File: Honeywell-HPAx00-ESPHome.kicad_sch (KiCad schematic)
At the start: 29 parts, among them J1 Conn_01x06, J2 Conn_01x01, J3 Conn_01x01, J4 Conn_01x01, J5 Conn_01x01, J6 Conn_01x01, J7 Conn_01x01, U1 mini_esp32

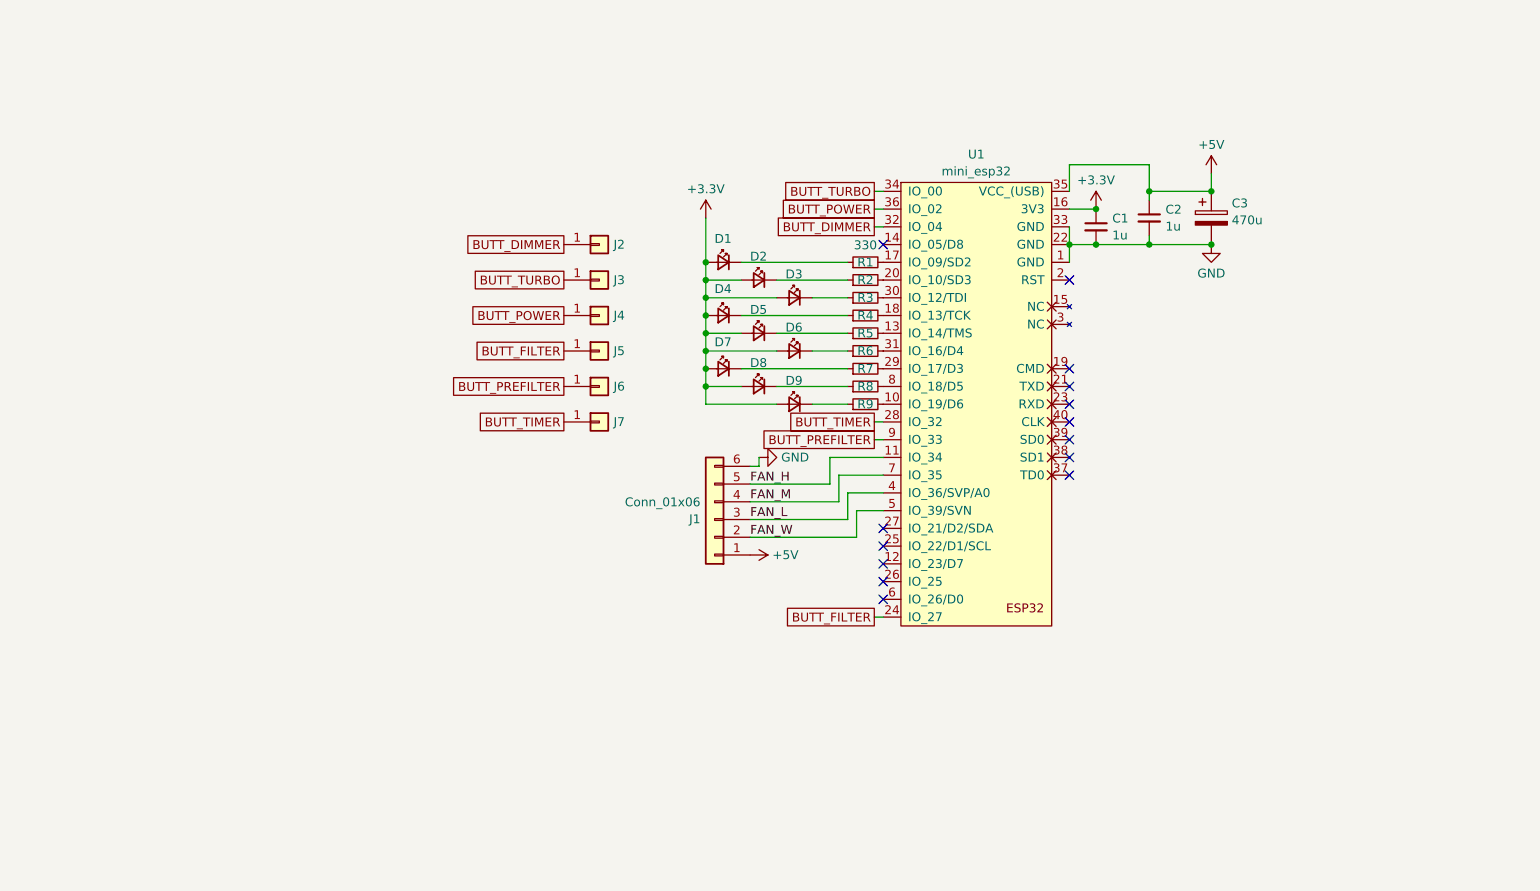
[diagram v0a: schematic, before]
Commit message: Update based on feedback
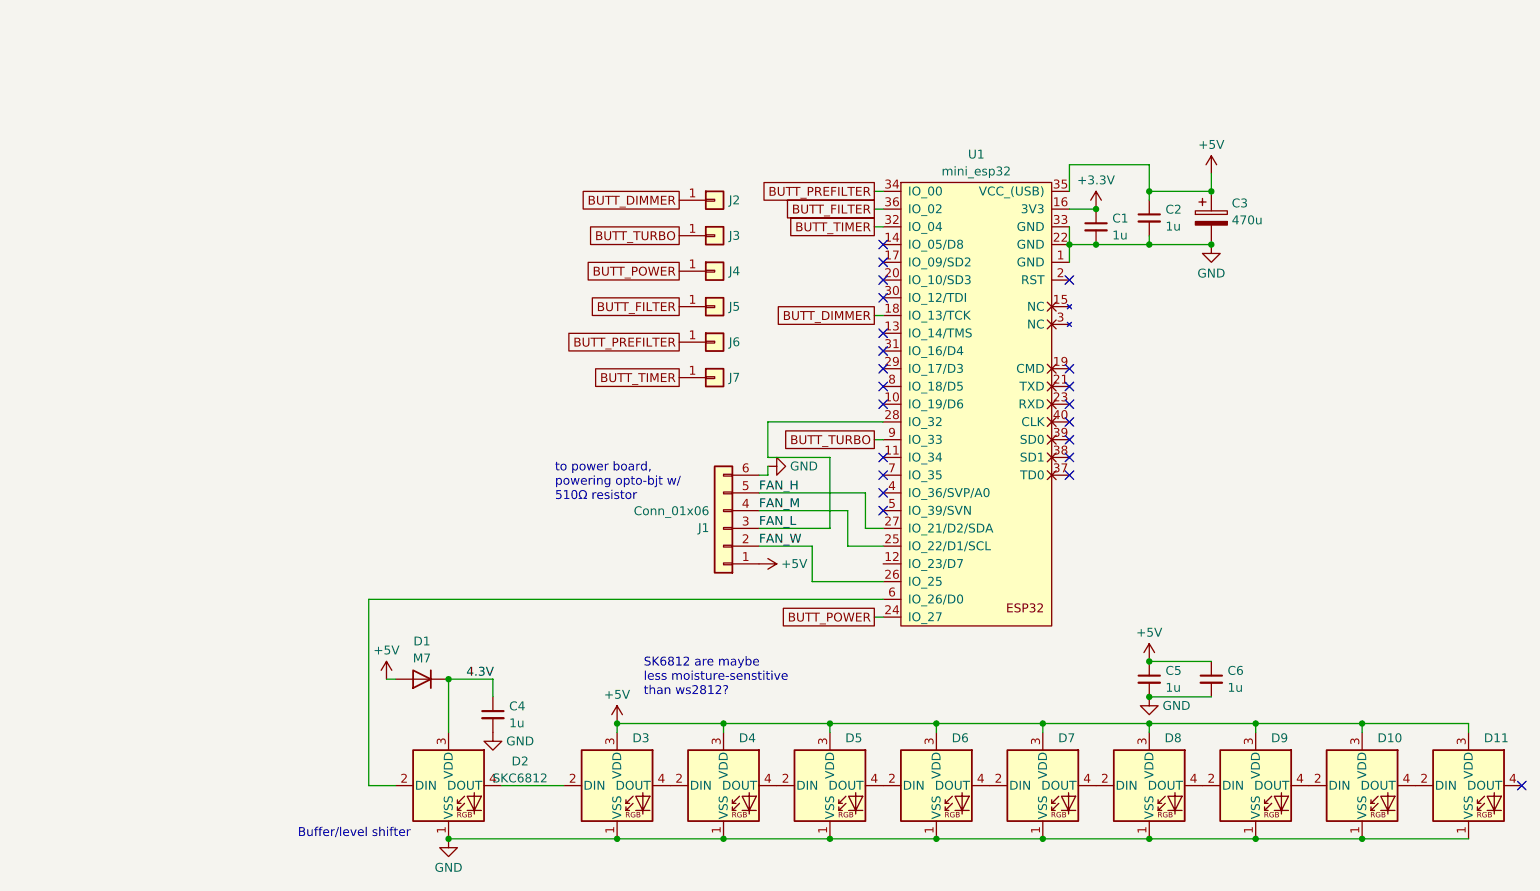
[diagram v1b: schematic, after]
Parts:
- removed D1, D2, D3, D4, D5, D6, D7, D8, D9: Red, LED_SMD:LED_0603_1608Metric_Pad1.05x0.95mm_HandSolder, symbol Device:LED_Small
- removed R1, R2, R3, R4, R5, R6, R7, R8, R9: 330, Resistor_SMD:R_0603_1608Metric_Pad0.98x0.95mm_HandSolder, symbol Device:R_Small
- added C4, C5, C6: 1u, Capacitor_SMD:C_0805_2012Metric_Pad1.18x1.45mm_HandSolder, symbol Device:C_Small
- added D1: M7, Diode_SMD:D_SMA_Handsoldering, symbol Device:D
- added D10, D11, D2, D3, D4, D5, D6, D7, D8, D9: SKC6812, LED_SMD:LED_SK6812_PLCC4_5.0x5.0mm_P3.2mm, symbol LED:SK6812
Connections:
- net +5V: now also C5.1, C6.1, D1.2 (A), D10.3 (VDD), D11.3 (VDD), D3.3 (VDD), D4.3 (VDD), D5.3 (VDD), D6.3 (VDD), D7.3 (VDD), D8.3 (VDD), D9.3 (VDD)
- net BUTT_DIMMER: now also U1.18 (IO_13/TCK); no longer U1.32 (IO_04)
- net BUTT_FILTER: now also U1.36 (IO_02); no longer U1.24 (IO_27)
- net BUTT_POWER: now also U1.24 (IO_27); no longer U1.36 (IO_02)
- net BUTT_PREFILTER: now also U1.34 (IO_00); no longer U1.9 (IO_33)
- net BUTT_TIMER: now also U1.32 (IO_04); no longer U1.28 (IO_32)
- net BUTT_TURBO: now also U1.9 (IO_33); no longer U1.34 (IO_00)
- net FAN_H: now also U1.27 (IO_21/D2/SDA); no longer U1.11 (IO_34)
- net FAN_L: now also U1.28 (IO_32); no longer U1.4 (IO_36/SVP/A0)
- net FAN_M: now also U1.25 (IO_22/D1/SCL); no longer U1.7 (IO_35)
- net FAN_W: now also U1.26 (IO_25); no longer U1.5 (IO_39/SVN)
- net GND: now also C4.2, C5.2, C6.2, D10.1 (VSS), D11.1 (VSS), D2.1 (VSS), D3.1 (VSS), D4.1 (VSS), D5.1 (VSS), D6.1 (VSS), D7.1 (VSS), D8.1 (VSS), D9.1 (VSS)
- net at U1.6 (IO_26/D0): now also D2.2 (DIN)
- new net: D8.4 (DOUT), D9.2 (DIN)
- new net: D10.2 (DIN), D9.4 (DOUT)
- new net: D6.4 (DOUT), D7.2 (DIN)
- new net: D7.4 (DOUT), D8.2 (DIN)
- new net: D4.4 (DOUT), D5.2 (DIN)
- new net: D5.4 (DOUT), D6.2 (DIN)
- new net: D10.4 (DOUT), D11.2 (DIN)
- new net: D3.4 (DOUT), D4.2 (DIN)
- new net: D2.4 (DOUT), D3.2 (DIN)
- new net 4.3V: C4.1, D1.1 (K), D2.3 (VDD)
- no-connect marks 14 -> 22
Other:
- note added: "Buffer/level shifter"
- note added: "SK6812 are maybe less moisture-senstitive than ws2812?"
- note added: "to power board, powering opto-bjt w/ 510Ω resistor"
- moved on the sheet: J1, J2, J3, J4, J5, J6, J7

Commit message: Update design
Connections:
- net BUTT_FILTER: now also U1.28 (IO_32); no longer U1.36 (IO_02)
- net BUTT_PREFILTER: now also U1.13 (IO_14/TMS); no longer U1.34 (IO_00)
- net BUTT_TIMER: now also U1.30 (IO_12/TDI); no longer U1.32 (IO_04)
- net FAN_H: now also U1.29 (IO_17/D3); no longer U1.27 (IO_21/D2/SDA)
- net FAN_L: now also U1.26 (IO_25); no longer U1.28 (IO_32)
- net FAN_W: now also U1.27 (IO_21/D2/SDA); no longer U1.26 (IO_25)
- net at D2.2 (DIN): now also U1.36 (IO_02); no longer U1.6 (IO_26/D0)
- no-connect marks 22 -> 23
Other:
- note added: "touch may be: IO00 IO02 IO04 IO12 IO13 IO14 IO15 IO27 IO32 IO33"
- moved on the sheet: J1, J2, J3, J4, J5, J6, J7

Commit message: final tweaks
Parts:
- J2, J3, J4, J5, J6, J7: footprint TestPoint:TestPoint_THTPad_D1.5mm_Drill0.7mm -> TestPoint:TestPoint_THTPad_D2.0mm_Drill1.0mm
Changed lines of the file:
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@@
       (effects (font (size 1.27 1.27)) (justify left) hide)
     )
-    (property "Footprint" "TestPoint:TestPoint_THTPad_D1.5mm_Drill0.7mm" (at 96.52 82.55 0)
+    (property "Footprint" "TestPoint:TestPoint_THTPad_D2.0mm_Drill1.0mm" (at 96.52 82.55 0)
       (effects (font (size 1.27 1.27)) hide)
     )
@@
       (effects (font (size 1.27 1.27)) (justify left) hide)
     )
-    (property "Footprint" "TestPoint:TestPoint_THTPad_D1.5mm_Drill0.7mm" (at 96.52 87.63 0)
+    (property "Footprint" "TestPoint:TestPoint_THTPad_D2.0mm_Drill1.0mm" (at 96.52 87.63 0)
       (effects (font (size 1.27 1.27)) hide)
     )
@@
       (effects (font (size 1.27 1.27)) (justify left) hide)
     )
-    (property "Footprint" "TestPoint:TestPoint_THTPad_D1.5mm_Drill0.7mm" (at 96.52 62.23 0)
+    (property "Footprint" "TestPoint:TestPoint_THTPad_D2.0mm_Drill1.0mm" (at 96.52 62.23 0)
       (effects (font (size 1.27 1.27)) hide)
     )
@@
       (effects (font (size 1.27 1.27)) (justify left) hide)
     )
-    (property "Footprint" "TestPoint:TestPoint_THTPad_D1.5mm_Drill0.7mm" (at 96.52 77.47 0)
+    (property "Footprint" "TestPoint:TestPoint_THTPad_D2.0mm_Drill1.0mm" (at 96.52 77.47 0)
       (effects (font (size 1.27 1.27)) hide)
     )
@@
       (effects (font (size 1.27 1.27)) (justify left) hide)
     )
-    (property "Footprint" "TestPoint:TestPoint_THTPad_D1.5mm_Drill0.7mm" (at 96.52 72.39 0)
+    (property "Footprint" "TestPoint:TestPoint_THTPad_D2.0mm_Drill1.0mm" (at 96.52 72.39 0)
       (effects (font (size 1.27 1.27)) hide)
     )
@@
       (effects (font (size 1.27 1.27)) (justify left) hide)
     )
-    (property "Footprint" "TestPoint:TestPoint_THTPad_D1.5mm_Drill0.7mm" (at 96.52 67.31 0)
-      (effects (font (size 1.27 1.27)) hide)
-    )
+    (property "Footprint" "TestPoint:TestPoint_THTPad_D2.0mm_Drill1.0mm" (at 96.52 67.31 0)
+      (effects (font (size 1.27 1.27)) hide)
+    )

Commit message: Fix issues from production
1. clear space around buttons on ground plane
2. increase capacitor to 4.7mF (1mF would be an absolute minimum)
3. increase hole size for connector, since it's a very tight fit
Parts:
- C3: value 470u -> 4700u; footprint Capacitor_THT:CP_Radial_D8.0mm_P3.50mm -> Capacitor_THT:CP_Radial_D12.5mm_P5.00mm; LCSC C6718380 -> C782984
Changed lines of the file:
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@@
       (effects (font (size 1.27 1.27)) (justify left))
     )
-    (property "Value" "470u" (at 195.961 57.4731 0)
+    (property "Value" "4700u" (at 195.961 57.4731 0)
       (effects (font (size 1.27 1.27)) (justify left))
     )
-    (property "Footprint" "Capacitor_THT:CP_Radial_D8.0mm_P3.50mm" (at 194.0052 60.96 0)
+    (property "Footprint" "Capacitor_THT:CP_Radial_D12.5mm_P5.00mm" (at 194.0052 60.96 0)
       (effects (font (size 1.27 1.27)) hide)
     )
@@
       (effects (font (size 1.27 1.27)) hide)
     )
-    (property "LCSC" "C6718380" (at 193.04 57.15 0)
+    (property "LCSC" "C782984" (at 193.04 57.15 0)
       (effects (font (size 1.27 1.27)) hide)
     )

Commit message: Update with complete instructions
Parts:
- C3: value 4700u -> 1000uF; footprint Capacitor_THT:CP_Radial_D12.5mm_P5.00mm -> Capacitor_THT:CP_Radial_D8.0mm_P3.50mm; LCSC C782984 -> C494544
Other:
- note added: "Mod the power supply board by replacing the 78L05 LDO with buck module"
- note removed: "touch may be: IO00 IO02 IO04 IO12 IO13 IO14 IO15 IO27 IO32 IO33"
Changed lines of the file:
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@@
   (junction (at 153.67 129.54) (diameter 0) (color 0 0 0 0)
   )
+  (junction (at 193.04 60.96) (diameter 0) (color 0 0 0 0)
+  )
   (junction (at 168.91 129.54) (diameter 0) (color 0 0 0 0)
   )
   (junction (at 168.91 146.05) (diameter 0) (color 0 0 0 0)
   )
+  (junction (at 193.04 53.34) (diameter 0) (color 0 0 0 0)
+  )
   (junction (at 184.15 120.65) (diameter 0) (color 0 0 0 0)
   )
@@
   (junction (at 184.15 129.54) (diameter 0) (color 0 0 0 0)
   )
-  (junction (at 193.04 53.34) (diameter 0) (color 0 0 0 0)
-  )
   (junction (at 184.15 146.05) (diameter 0) (color 0 0 0 0)
   )
@@
   )
   (junction (at 176.53 60.96) (diameter 0) (color 0 0 0 0)
-  )
-  (junction (at 193.04 60.96) (diameter 0) (color 0 0 0 0)
   )
   (junction (at 153.67 146.05) (diameter 0) (color 0 0 0 0)
@@
     (stroke (width 0) (type default))
   )
+  (rectangle (start 100.33 39.37) (end 134.62 50.8)
+    (stroke (width 0) (type default))
+    (fill (type none))
+  )
   (text "Buffer/level shifter" (at 62.23 146.05 0)
     (effects (font (size 1.27 1.27)) (justify left bottom) (href "https://hackaday.com/2017/01/20/cheating-at-5v-ws2812-control-to-use-a-3-3v-data-line/"))
@@
     (effects (font (size 1.27 1.27)) (justify left bottom))
   )
-  (text "touch may be:\nIO00 IO02 IO04 IO12 IO13\nIO14 IO15 IO27 IO32 IO33"
-    (at 125.73 41.91 0)
+  (text "Mod the power supply board\nby replacing the 78L05 LDO\nwith buck module"
+    (at 102.87 48.26 0)
     (effects (font (size 1.27 1.27)) (justify left bottom))
   )
@@
         (path "/1129a227-3bd7-4f69-9cc1-be30ea3885e9"
           (reference "C5") (unit 1)
+        )
+      )
+    )
+  )
+  (symbol (lib_id "power:+5V") (at 128.27 111.76 270) (unit 1)
+    (in_bom yes) (on_board yes) (dnp no) (fields_autoplaced)
+    (property "Reference" "#PWR014" (at 124.46 111.76 0)
+      (effects (font (size 1.27 1.27)) hide)
+    )
+    (property "Value" "+5V" (at 131.445 111.76 90)
+      (effects (font (size 1.27 1.27)) (justify left))
+    )
+    (property "Footprint" "" (at 128.27 111.76 0)
+      (effects (font (size 1.27 1.27)) hide)
+    )
+    (property "Datasheet" "" (at 128.27 111.76 0)
+      (effects (font (size 1.27 1.27)) hide)
+    )
+    (pin "1")
+    (instances
+      (project "Honeywell-HPAx00-ESPHome"
+        (path "/1129a227-3bd7-4f69-9cc1-be30ea3885e9"
+          (reference "#PWR014") (unit 1)
         )
       )
@@
       (effects (font (size 1.27 1.27)) (justify left))
     )
-    (property "Value" "4700u" (at 195.961 57.4731 0)
-      (effects (font (size 1.27 1.27)) (justify left))
-    )
-    (property "Footprint" "Capacitor_THT:CP_Radial_D12.5mm_P5.00mm" (at 194.0052 60.96 0)
+    (property "Value" "1000uF" (at 195.961 57.4731 0)
+      (effects (font (size 1.27 1.27)) (justify left))
+    )
+    (property "Footprint" "Capacitor_THT:CP_Radial_D8.0mm_P3.50mm" (at 194.0052 60.96 0)
       (effects (font (size 1.27 1.27)) hide)
     )
@@
       (effects (font (size 1.27 1.27)) hide)
     )
-    (property "LCSC" "C782984" (at 193.04 57.15 0)
+    (property "LCSC" "C494544" (at 193.04 57.15 0)
       (effects (font (size 1.27 1.27)) hide)
     )
@@
         )
       )
-    )
-  )
-  (symbol (lib_id "power:+5V") (at 128.27 111.76 270) (mirror x) (unit 1)
-    (in_bom yes) (on_board yes) (dnp no) (fields_autoplaced)
-    (property "Reference" "#PWR02" (at 124.46 111.76 0)
-      (effects (font (size 1.27 1.27)) hide)
-    )
-    (property "Value" "+5V" (at 131.4449 111.76 90)
-      (effects (font (size 1.27 1.27)) (justify left))
-    )
-    (property "Footprint" "" (at 128.27 111.76 0)
-      (effects (font (size 1.27 1.27)) hide)
-    )
-    (property "Datasheet" "" (at 128.27 111.76 0)
-      (effects (font (size 1.27 1.27)) hide)
-    )
-    (pin "1")
-    (instances
-      (project "Honeywell-HPAx00-ESPHome"
-        (path "/1129a227-3bd7-4f69-9cc1-be30ea3885e9"
-          (reference "#PWR02") (unit 1)
-        )
-      )

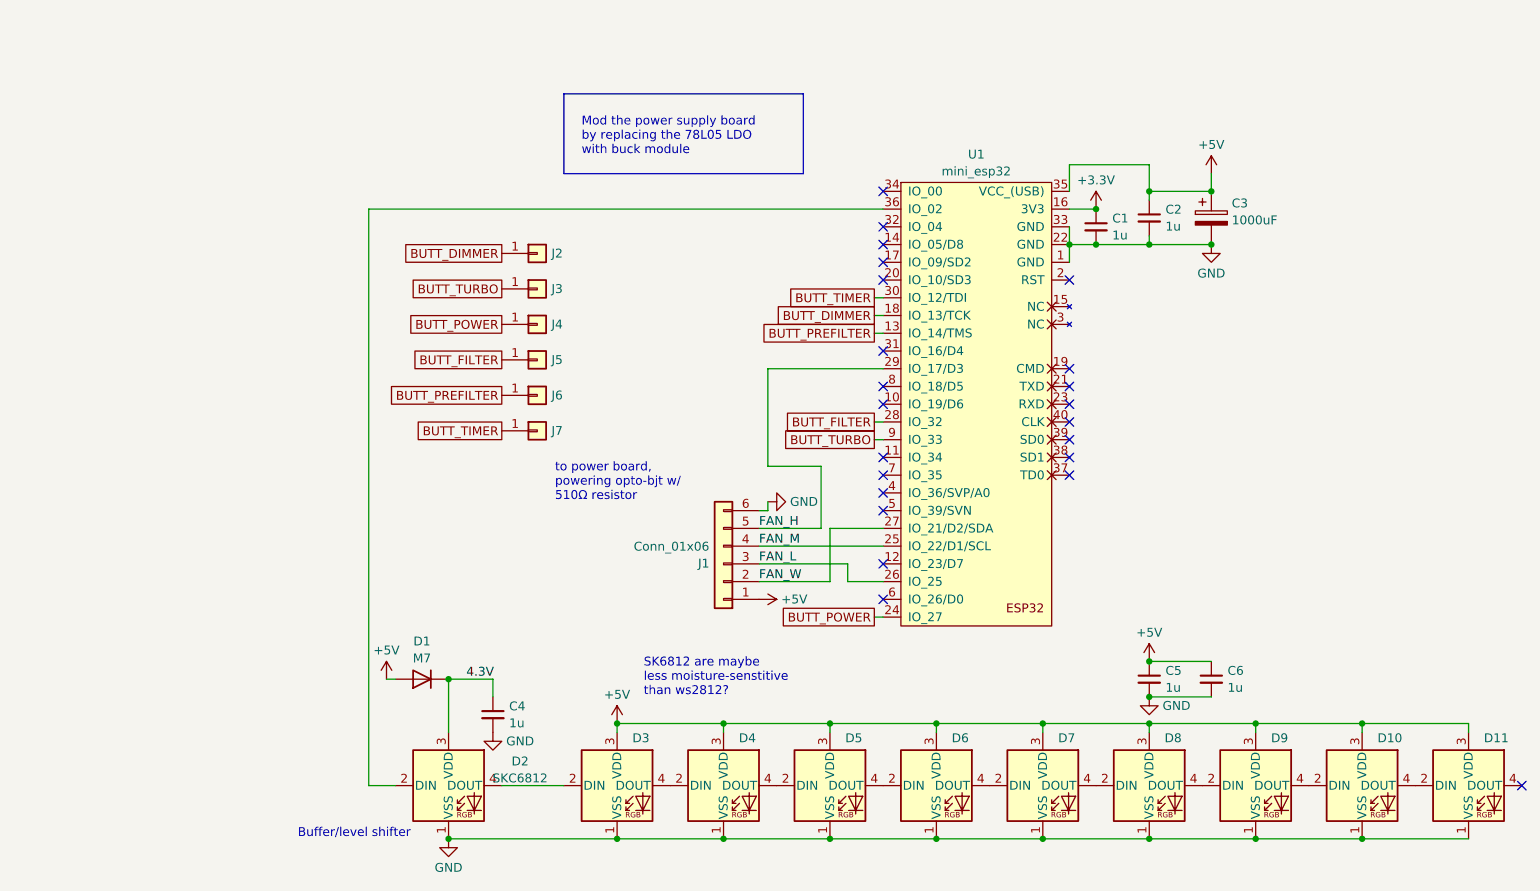
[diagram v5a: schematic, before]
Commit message: Add connector for extra 5V PSU
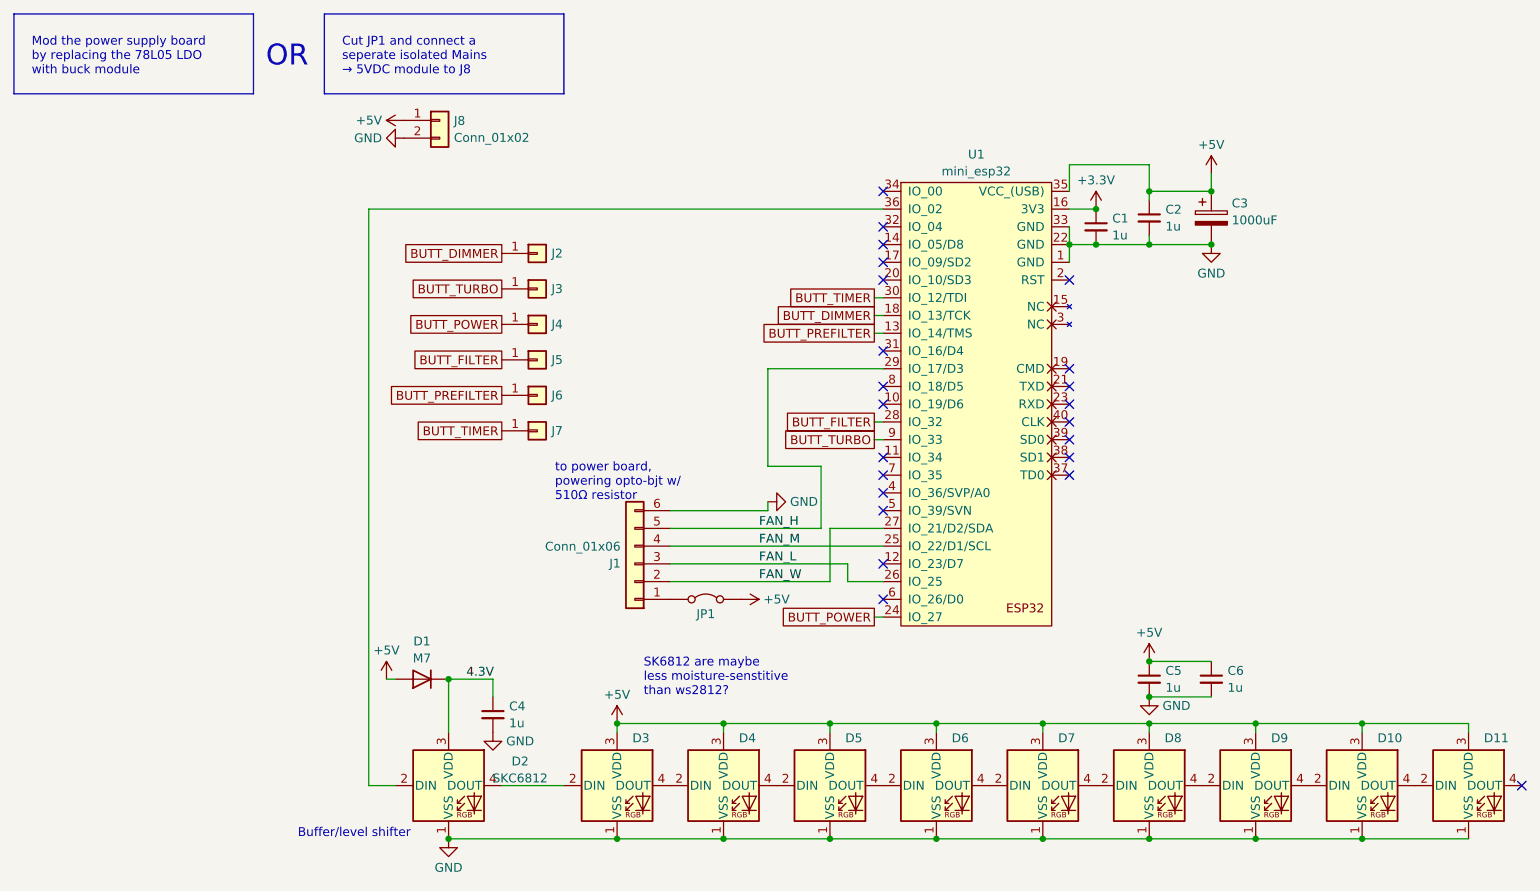
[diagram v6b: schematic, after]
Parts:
- added J8: Conn_01x02, Connector_Wire:SolderWire-0.5sqmm_1x02_P4.6mm_D0.9mm_OD2.1mm_Relief, symbol Connector_Generic:Conn_01x02
- added JP1: Jumper_2_Bridged, Jumper:SolderJumper-2_P1.3mm_Bridged_RoundedPad1.0x1.5mm, symbol Jumper:Jumper_2_Bridged
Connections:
- net +5V: now also J8.1 (Pin_1), JP1.2 (B); no longer J1.1 (Pin_1)
- net GND: now also J8.2 (Pin_2)
- new net: J1.1 (Pin_1), JP1.1 (A)
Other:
- note added: "Cut JP1 and connect a seperate isolated Mains → 5VDC module to J8"
- note added: "OR"
- moved on the sheet: J1
